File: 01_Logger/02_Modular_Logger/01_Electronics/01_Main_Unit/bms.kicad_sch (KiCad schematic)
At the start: 54 parts, among them IC801 BQ40Z80, J801 Conn_01x02_Male, J802 Conn_01x05_Male, J803 Conn_01x05_Female, K801 2N7002KW, K802 CSD18540Q5B, K803 DMP6023LSS-13, K804 CSD18540Q5B, SW801 SW_Push

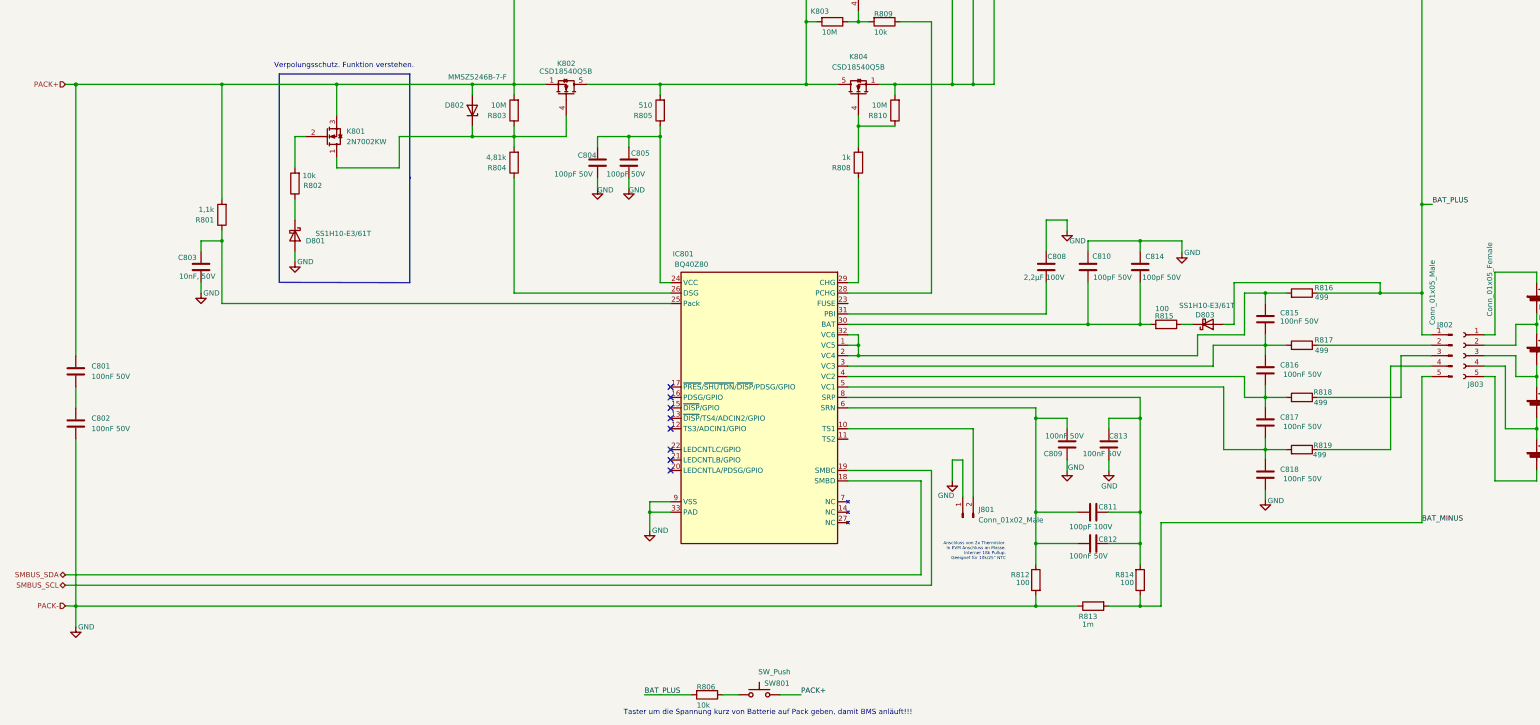
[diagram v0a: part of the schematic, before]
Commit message: update Electronics for Modular_Logger
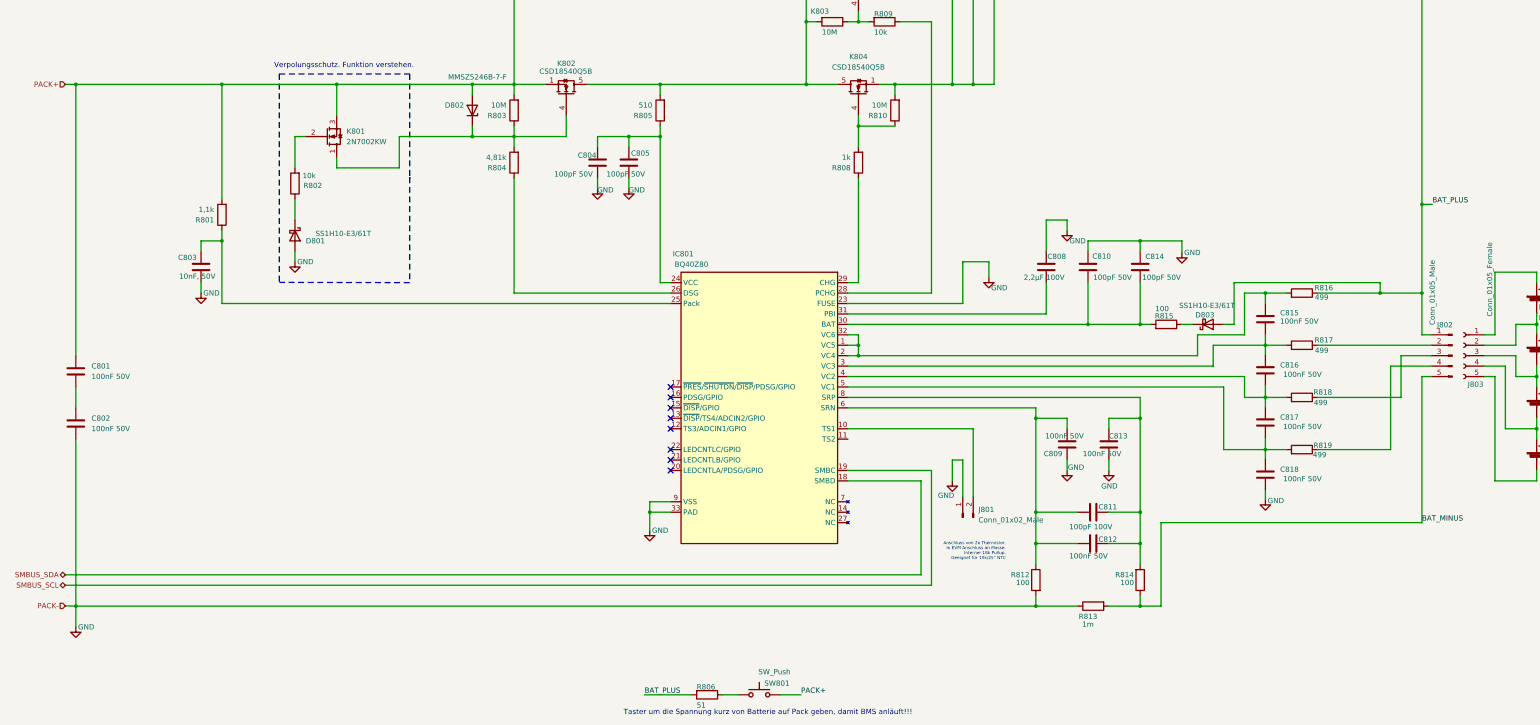
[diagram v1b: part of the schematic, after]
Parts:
- R806: value 10k -> 51
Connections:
- net GND: now also IC801.23 (FUSE)
